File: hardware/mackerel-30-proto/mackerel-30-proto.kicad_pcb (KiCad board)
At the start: 2 copper layers, 24 parts, among them U1 MC68030RC, U2 EPM7128, U3 SST39SF040, U4 AS6C4008-55PCN

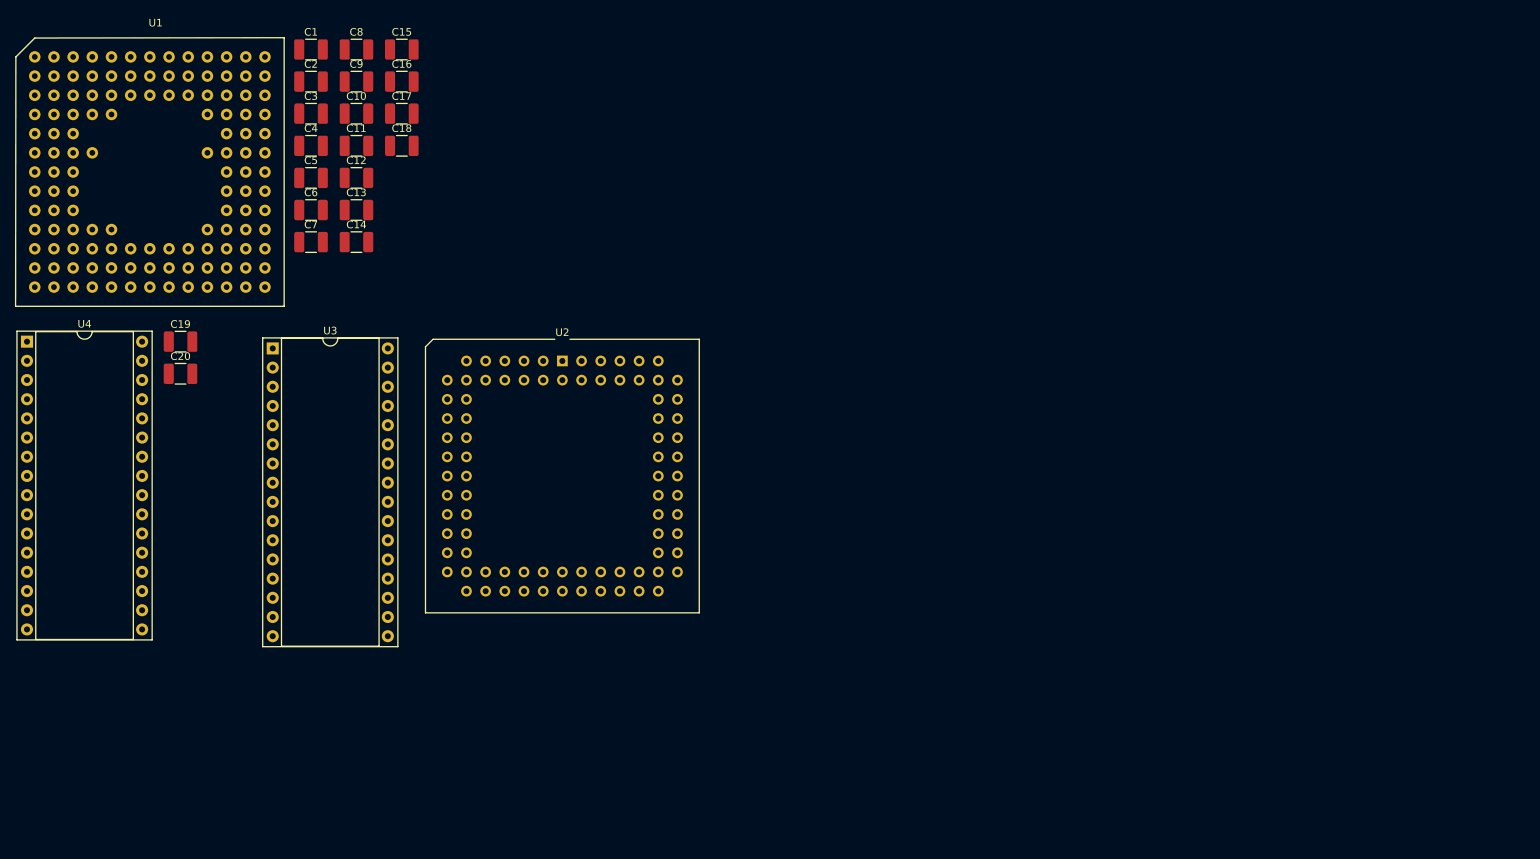
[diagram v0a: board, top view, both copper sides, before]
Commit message: Add power and DUART
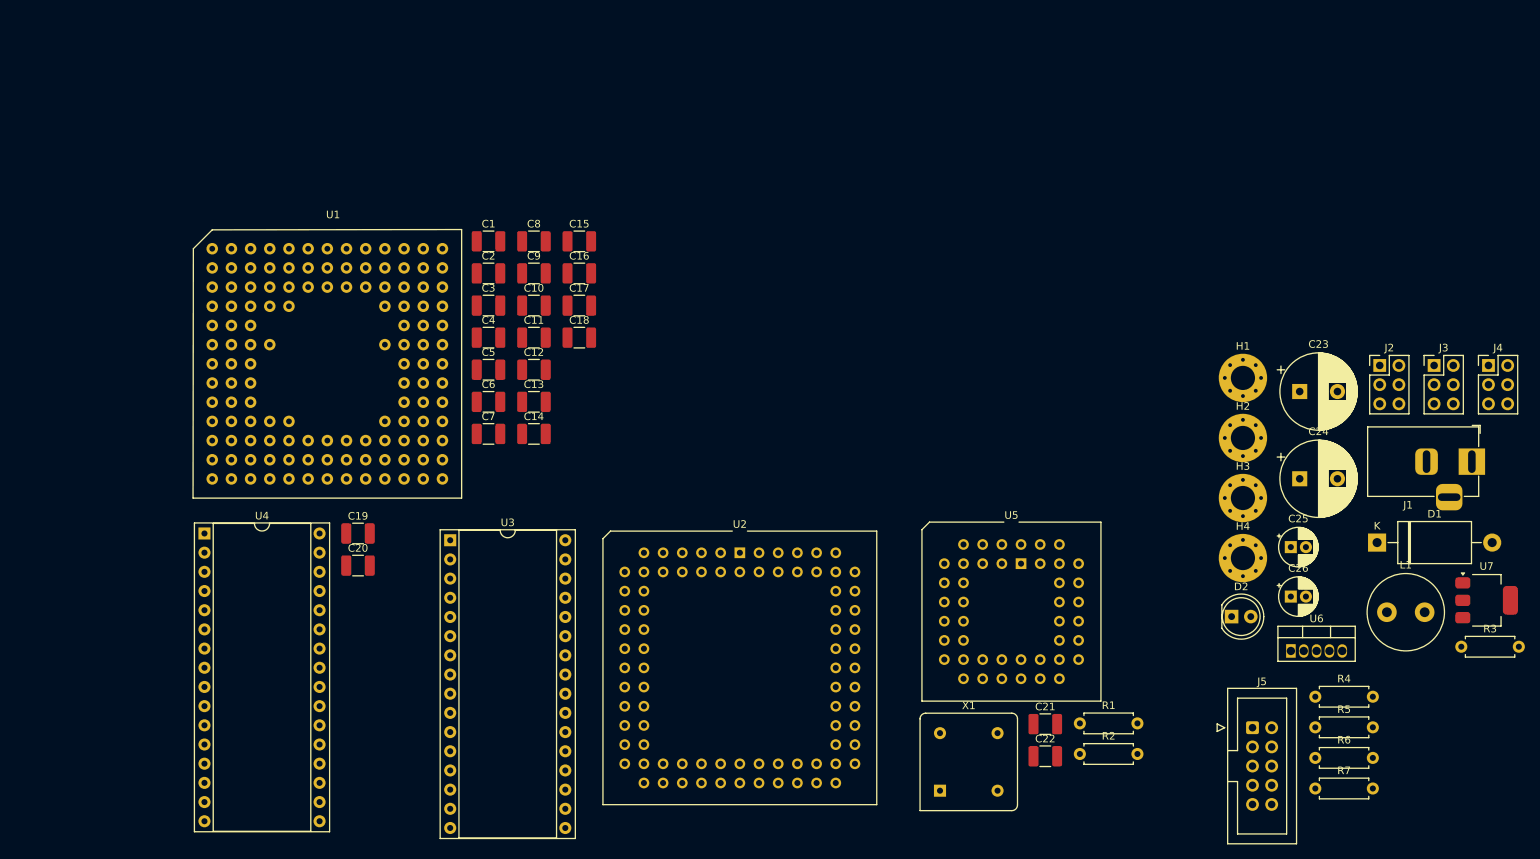
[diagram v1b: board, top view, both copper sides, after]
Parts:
- added C21: 0.1uF, Capacitor_SMD:C_1210_3225Metric_Pad1.33x2.70mm_HandSolder, F.Cu at (136.4, 90.9)
- added C22: 0.1uF, Capacitor_SMD:C_1210_3225Metric_Pad1.33x2.70mm_HandSolder, F.Cu at (136.4, 95.2)
- added C23: 1000uF, Capacitor_THT:CP_Radial_D10.0mm_P5.00mm, F.Cu at (170.1, 46.9)
- added C24: 1000uF, Capacitor_THT:CP_Radial_D10.0mm_P5.00mm, F.Cu at (170.1, 58.5)
- added C25: 10uF, Capacitor_THT:CP_Radial_D5.0mm_P2.00mm, F.Cu at (168.9, 67.5)
- added C26: 10uF, Capacitor_THT:CP_Radial_D5.0mm_P2.00mm, F.Cu at (168.9, 74.1)
- added D1: 1N5822, Diode_THT:D_DO-27_P15.24mm_Horizontal, F.Cu at (180.3, 66.9)
- added D2: LED, LED_THT:LED_D5.0mm, F.Cu at (161.1, 76.7)
- added H1: MountingHole_Pad, MountingHole:MountingHole_3.2mm_M3_Pad_Via, F.Cu at (162.6, 45.1)
- added H2: MountingHole_Pad, MountingHole:MountingHole_3.2mm_M3_Pad_Via, F.Cu at (162.6, 53.1)
- added H3: MountingHole_Pad, MountingHole:MountingHole_3.2mm_M3_Pad_Via, F.Cu at (162.6, 61.0)
- added H4: MountingHole_Pad, MountingHole:MountingHole_3.2mm_M3_Pad_Via, F.Cu at (162.6, 69.0)
- added J1: Barrel_Jack_MountingPin, Connector_BarrelJack:BarrelJack_Horizontal, F.Cu at (192.9, 56.2)
- added J2: Conn_02x03_Odd_Even, Connector_PinHeader_2.54mm:PinHeader_2x03_P2.54mm_Vertical, F.Cu at (180.7, 43.5)
- added J3: Conn_02x03_Odd_Even, Connector_PinHeader_2.54mm:PinHeader_2x03_P2.54mm_Vertical, F.Cu at (187.9, 43.5)
- added J4: Conn_02x03_Odd_Even, Connector_PinHeader_2.54mm:PinHeader_2x03_P2.54mm_Vertical, F.Cu at (195.1, 43.5)
- added J5: Conn_02x05_Odd_Even, Connector_IDC:IDC-Header_2x05_P2.54mm_Vertical, F.Cu at (163.8, 91.4)
- added L1: 100uH, Inductor_THT:L_Radial_D10.0mm_P5.00mm_Fastron_07M, F.Cu at (181.6, 76.1)
- added R1: R, Resistor_THT:R_Axial_DIN0207_L6.3mm_D2.5mm_P7.62mm_Horizontal, F.Cu at (141.0, 90.8)
- added R2: R, Resistor_THT:R_Axial_DIN0207_L6.3mm_D2.5mm_P7.62mm_Horizontal, F.Cu at (141.0, 94.9)
- added R3: 1k, Resistor_THT:R_Axial_DIN0207_L6.3mm_D2.5mm_P7.62mm_Horizontal, F.Cu at (191.5, 80.7)
- added R4: R, Resistor_THT:R_Axial_DIN0207_L6.3mm_D2.5mm_P7.62mm_Horizontal, F.Cu at (172.1, 87.3)
- added R5: R, Resistor_THT:R_Axial_DIN0207_L6.3mm_D2.5mm_P7.62mm_Horizontal, F.Cu at (172.1, 91.4)
- added R6: R, Resistor_THT:R_Axial_DIN0207_L6.3mm_D2.5mm_P7.62mm_Horizontal, F.Cu at (172.1, 95.4)
- added R7: R, Resistor_THT:R_Axial_DIN0207_L6.3mm_D2.5mm_P7.62mm_Horizontal, F.Cu at (172.1, 99.5)
- added U5: XR68C681, Package_LCC:PLCC-44_THT-Socket, F.Cu at (133.2, 69.7)
- added U6: LM2576T-5, Package_TO_SOT_THT:TO-220-5_Vertical, F.Cu at (168.9, 81.3)
- added U7: AMS1117-3.3, Package_TO_SOT_SMD:SOT-223-3_TabPin2, F.Cu at (194.8, 74.6)
- added X1: 3.6864MHz, Oscillator:Oscillator_DIP-8, F.Cu at (122.5, 99.8)
- moved U2 34.6 mm to (96.0, 68.3)
- moved C10 34.6 mm to (68.7, 35.5)
- moved C11 34.6 mm to (68.7, 39.8)
- moved C12 34.6 mm to (68.7, 44.0)
- moved C13 34.6 mm to (68.7, 48.3)
- moved C14 34.6 mm to (68.7, 52.5)
- moved C17 34.6 mm to (74.7, 35.5)
- moved C18 34.6 mm to (74.7, 39.8)
- moved C3 34.6 mm to (62.7, 35.5)
- moved C4 34.6 mm to (62.7, 39.8)
- moved C5 34.6 mm to (62.7, 44.0)
- moved C6 34.6 mm to (62.7, 48.3)
- moved C7 34.6 mm to (62.7, 52.5)
- moved U3 34.6 mm to (57.6, 66.6)
- moved C1 34.6 mm to (62.7, 27.0)
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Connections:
- U2 pad 14: unconnected-(U2-TDI-Pad14) -> TDI
- U2 pad 23: unconnected-(U2-TMS-Pad23) -> TMS
- U2 pad 62: unconnected-(U2-TCK-Pad62) -> TCK
- U2 pad 71: unconnected-(U2-TDO-Pad71) -> TDO

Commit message: Add 68882 FPU symbol
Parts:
- removed R5: R, Resistor_THT:R_Axial_DIN0207_L6.3mm_D2.5mm_P7.62mm_Horizontal
- added J6: Conn_02x05_Odd_Even, Connector_IDC:IDC-Header_2x05_P2.54mm_Vertical, F.Cu at (-90.8, 30.1)
- added R10: R, Resistor_THT:R_Axial_DIN0207_L6.3mm_D2.5mm_P7.62mm_Horizontal, F.Cu at (-82.5, 30.1)
- added R11: R, Resistor_THT:R_Axial_DIN0207_L6.3mm_D2.5mm_P7.62mm_Horizontal, F.Cu at (-82.5, 34.1)
- added R12: R, Resistor_THT:R_Axial_DIN0207_L6.3mm_D2.5mm_P7.62mm_Horizontal, F.Cu at (-82.5, 38.2)
- added R8: 1k, Resistor_THT:R_Axial_DIN0207_L6.3mm_D2.5mm_P7.62mm_Horizontal, F.Cu at (-38.4, 147.9)
- added R9: R, Resistor_THT:R_Axial_DIN0207_L6.3mm_D2.5mm_P7.62mm_Horizontal, F.Cu at (-82.5, 26.0)
- added U10: MC68882, Package_LCC:PLCC-68_THT-Socket, F.Cu at (-121.9, 59.7)
- added U8: EPM7128, Package_LCC:PLCC-84_THT-Socket, F.Cu at (176.4, 30.0)
- added U9: SIMM72, mackerel:SIMM-72, F.Cu at (208.6, 32.3)
- C24: value 1000uF -> 10uF; footprint Capacitor_THT:CP_Radial_D10.0mm_P5.00mm -> Capacitor_THT:CP_Radial_D5.0mm_P2.00mm
- C25: value 10uF -> 1000uF; footprint Capacitor_THT:CP_Radial_D5.0mm_P2.00mm -> Capacitor_THT:CP_Radial_D10.0mm_P5.00mm
- D1: value 1N5822 -> LED; footprint Diode_THT:D_DO-27_P15.24mm_Horizontal -> LED_THT:LED_D5.0mm
- D2: value LED -> 1N5822; footprint LED_THT:LED_D5.0mm -> Diode_THT:D_DO-27_P15.24mm_Horizontal
- J1: value Barrel_Jack_MountingPin -> Conn_02x05_Odd_Even; footprint Connector_BarrelJack:BarrelJack_Horizontal -> Connector_IDC:IDC-Header_2x05_P2.54mm_Vertical
- J2: value Conn_02x03_Odd_Even -> Barrel_Jack_MountingPin; footprint Connector_PinHeader_2.54mm:PinHeader_2x03_P2.54mm_Vertical -> Connector_BarrelJack:BarrelJack_Horizontal
- J5: value Conn_02x05_Odd_Even -> Conn_02x03_Odd_Even; footprint Connector_IDC:IDC-Header_2x05_P2.54mm_Vertical -> Connector_PinHeader_2.54mm:PinHeader_2x03_P2.54mm_Vertical
- R3: value 1k -> R
- U4: footprint Package_DIP:DIP-32_W15.24mm_Socket -> Package_DIP:DIP-32_W15.24mm
- moved J1 284.0 mm to (-90.8, 70.2)
- moved R3 274.1 mm to (-82.5, 74.2)
- moved D1 260.8 mm to (-68.8, 144.0)
- moved R4 254.8 mm to (-82.5, 78.2)
- moved J4 246.5 mm to (-42.0, 110.7)
- moved J3 246.5 mm to (-49.2, 110.7)
- moved C24 243.3 mm to (-61.0, 134.8)
- moved C23 239.5 mm to (-59.8, 114.2)
- moved C26 239.5 mm to (-61.0, 141.3)
- moved H1 239.5 mm to (-67.3, 112.4)
- moved H2 239.5 mm to (-67.3, 120.3)
- moved H3 239.5 mm to (-67.3, 128.3)
- moved H4 239.5 mm to (-67.3, 136.2)
- moved L1 239.5 mm to (-48.3, 143.4)
- moved U6 239.5 mm to (-61.0, 148.5)
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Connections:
- D1 pad 1: Net-(D1-K) -> GND
- D1 pad 2: GND -> Net-(D1-A)
- D2 pad 1: GND -> Net-(D2-K)
- D2 pad 2: Net-(D2-A) -> GND
- J1 pad 1: +12V -> TCK
- J1 pad 3: (no net) -> TDO
- J2 pad 3: +12V -> (no net)
- J3 pad 1: +5V -> +12V
- J3 pad 3: +5V -> +12V
- J3 pad 5: +5V -> +12V
- J4 pad 1: +3.3V -> +5V
- J4 pad 3: +3.3V -> +5V
- J4 pad 5: +3.3V -> +5V
- J5 pad 1: TCK -> +3.3V
- J5 pad 3: TDO -> +3.3V
- J5 pad 4: +5V -> GND
- J5 pad 5: TMS -> +3.3V
- J5 pad 6: unconnected-(J5-Pin_6-Pad6) -> GND
- L1 pad 1: Net-(D1-K) -> Net-(D2-K)
- R1 pad 1: Net-(U5-/IACK) -> +5V
- R1 pad 2: +5V -> TDO
- R2 pad 1: Net-(U5-INTR) -> +5V
- R2 pad 2: +5V -> TMS
- R3 pad 2: Net-(D2-A) -> TDI
- R4 pad 1: +5V -> TCK
- R4 pad 2: TDO -> GND
- R6 pad 1: +5V -> Net-(U5-/IACK)
- R6 pad 2: TDI -> +5V
- R7 pad 1: TCK -> Net-(U5-INTR)
- R7 pad 2: GND -> +5V
- U3 pad 22: unconnected-(U3-CE-Pad22) -> /CS_ROM
- U3 pad 24: unconnected-(U3-OE-Pad24) -> GND
- U3 pad 31: unconnected-(U3-PGM-Pad31) -> Net-(U3-PGM)
- U4 pad 22: unconnected-(U4-CE#-Pad22) -> /CS_SRAM
- U4 pad 24: unconnected-(U4-OE#-Pad24) -> GND
- U6 pad 2: Net-(D1-K) -> Net-(D2-K)
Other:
- board outline added: 200 x 120 mm

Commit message: Wired most of the control signals for the CPU and DRAM
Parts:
- removed J5: Conn_02x03_Odd_Even, Connector_PinHeader_2.54mm:PinHeader_2x03_P2.54mm_Vertical
- removed J6: Conn_02x05_Odd_Even, Connector_IDC:IDC-Header_2x05_P2.54mm_Vertical
- added J10: DE9_Plug_MountingHoles, Connector_Dsub:DSUB-9_Male_Horizontal_P2.77x2.84mm_EdgePinOffset7.70mm_Housed_MountingHolesOffset9.12mm, F.Cu at (30.8, 86.0)
- added J8: Conn_02x05_Odd_Even, Connector_IDC:IDC-Header_2x05_P2.54mm_Vertical, F.Cu at (260.9, 58.8)
- added J9: DE9_Plug_MountingHoles, Connector_Dsub:DSUB-9_Male_Horizontal_P2.77x2.84mm_EdgePinOffset7.70mm_Housed_MountingHolesOffset9.12mm, F.Cu at (30.8, 46.0)
- added R13: R, Resistor_THT:R_Axial_DIN0207_L6.3mm_D2.5mm_P7.62mm_Horizontal, F.Cu at (255.6, 119.6)
- added R14: 4k7, Resistor_THT:R_Axial_DIN0207_L6.3mm_D2.5mm_P7.62mm_Horizontal, F.Cu at (-97.8, 157.7)
- added R15: R, Resistor_THT:R_Axial_DIN0207_L6.3mm_D2.5mm_P7.62mm_Horizontal, F.Cu at (-91.7, 65.8)
- added R16: R, Resistor_THT:R_Axial_DIN0207_L6.3mm_D2.5mm_P7.62mm_Horizontal, F.Cu at (-91.7, 69.9)
- added R17: 1k, Resistor_THT:R_Axial_DIN0207_L6.3mm_D2.5mm_P7.62mm_Horizontal, F.Cu at (-77.5, 97.3)
- added R18: R, Resistor_THT:R_Axial_DIN0207_L6.3mm_D2.5mm_P7.62mm_Horizontal, F.Cu at (269.2, 54.6)
- added R19: R, Resistor_THT:R_Axial_DIN0207_L6.3mm_D2.5mm_P7.62mm_Horizontal, F.Cu at (269.2, 58.7)
- added R20: R, Resistor_THT:R_Axial_DIN0207_L6.3mm_D2.5mm_P7.62mm_Horizontal, F.Cu at (269.2, 62.8)
- added R21: R, Resistor_THT:R_Axial_DIN0207_L6.3mm_D2.5mm_P7.62mm_Horizontal, F.Cu at (269.2, 66.8)
- added R5: 4k7, Resistor_THT:R_Axial_DIN0207_L6.3mm_D2.5mm_P7.62mm_Horizontal, F.Cu at (-190.3, 82.0)
- added U11: MAX232, Package_DIP:DIP-16_W7.62mm_Socket, F.Cu at (112.1, -77.1)
- added U12: MAX232, Package_DIP:DIP-16_W7.62mm_Socket, F.Cu at (123.9, -77.1)
- added X2: 3.6864MHz, Oscillator:Oscillator_DIP-8, F.Cu at (139.7, -68.2)
- J1: value Conn_02x05_Odd_Even -> Conn_01x02; footprint Connector_IDC:IDC-Header_2x05_P2.54mm_Vertical -> Connector_PinHeader_2.54mm:PinHeader_1x02_P2.54mm_Vertical
- J2: value Barrel_Jack_MountingPin -> Conn_01x02; footprint Connector_BarrelJack:BarrelJack_Horizontal -> Connector_PinHeader_2.54mm:PinHeader_1x02_P2.54mm_Vertical
- J3: value Conn_02x03_Odd_Even -> Conn_02x05_Odd_Even; footprint Connector_PinHeader_2.54mm:PinHeader_2x03_P2.54mm_Vertical -> Connector_IDC:IDC-Header_2x05_P2.54mm_Vertical
- J4: value Conn_02x03_Odd_Even -> Barrel_Jack_MountingPin; footprint Connector_PinHeader_2.54mm:PinHeader_2x03_P2.54mm_Vertical -> Connector_BarrelJack:BarrelJack_Horizontal
- R1, R2, R3, R4, R6, R7, R9: value R -> 4k7
- R8: value 1k -> 4k7
- X1: value 3.6864MHz -> CXO_DIP14; footprint Oscillator:Oscillator_DIP-8 -> Oscillator:Oscillator_DIP-14
- moved R10 346.9 mm to (255.6, 107.5)
- moved R11 346.9 mm to (255.6, 111.5)
- moved R12 346.9 mm to (255.6, 115.5)
- moved J3 320.4 mm to (271.2, 108.8)
- moved H2 269.3 mm to (185.1, 26.4)
- moved H4 256.9 mm to (185.1, 183.8)
- moved U10 237.9 mm to (109.1, 116.7)
- moved U1 226.4 mm to (90.6, 58.7)
- moved U5 212.0 mm to (124.4, -46.5)
- moved U6 191.7 mm to (18.3, -26.0)
- moved R6 191.5 mm to (-190.3, 86.1)
- moved R7 191.5 mm to (-190.3, 90.2)
- moved L1 191.1 mm to (46.0, -22.8)
- moved C23 171.8 mm to (36.1, -28.4)
- moved C25 171.8 mm to (36.1, -16.8)
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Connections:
- J1 pad 1: TCK -> Net-(J1-Pin_1)
- J2 pad 1: +12V -> Net-(J2-Pin_1)
- J3 pad 1: +12V -> TCK
- J3 pad 3: +12V -> TDO
- J3 pad 4: GND -> +5V
- J3 pad 5: +12V -> TMS
- J3 pad 6: GND -> unconnected-(J3-Pin_6-Pad6)
- J4 pad 1: +5V -> +12V
- J4 pad 3: +5V -> (no net)
- R1 pad 2: TDO -> Net-(J2-Pin_1)
- R10 pad 2: TMS_DRAM -> TDO
- R11 pad 2: TDI_DRAM -> TMS
- R12 pad 1: TCK_DRAM -> +5V
- R12 pad 2: GND -> TDI
- R2 pad 2: TMS -> Net-(U1-/CBACK)
- R3 pad 2: TDI -> Net-(J1-Pin_1)
- R4 pad 1: TCK -> +5V
- R4 pad 2: GND -> Net-(U1-/HALT)
- R6 pad 1: Net-(U5-/IACK) -> +5V
- R6 pad 2: +5V -> /IPL1
- R7 pad 1: Net-(U5-INTR) -> +5V
- R7 pad 2: +5V -> /IPL2
- R8 pad 2: Net-(D1-A) -> Net-(U1-/BR)
- R9 pad 2: TDO_DRAM -> Net-(U1-/BGACK)
- U1 pad A1: unconnected-(U1-/BR-PadA1) -> Net-(U1-/BR)
- U1 pad A3: A30 -> unconnected-(U1-A30-PadA3)
- U1 pad A4: A28 -> unconnected-(U1-A28-PadA4)
- U1 pad B3: A31 -> unconnected-(U1-A31-PadB3)
- U1 pad B4: A29 -> unconnected-(U1-A29-PadB4)
- U1 pad C3: unconnected-(U1-/BGACK-PadC3) -> Net-(U1-/BGACK)
- U1 pad E1: unconnected-(U1-CLK-PadE1) -> CLK_CPU
- U1 pad F12: unconnected-(U1-/RESET-PadF12) -> /RESET
- U1 pad F13: unconnected-(U1-/MMUDIS-PadF13) -> Net-(J1-Pin_1)
- U1 pad G1: unconnected-(U1-/STERM-PadG1) -> /STERM
- U1 pad H1: unconnected-(U1-/BERR-PadH1) -> /BERR
- U1 pad H12: unconnected-(U1-/CDIS-PadH12) -> Net-(J2-Pin_1)
- U1 pad H2: unconnected-(U1-/HALT-PadH2) -> Net-(U1-/HALT)
- U1 pad J1: unconnected-(U1-/CBACK-PadJ1) -> Net-(U1-/CBACK)
- U1 pad L1: unconnected-(U1-/CIIN-PadL1) -> /CIIN
- U10 pad 13: unconnected-(U10-/RESET-Pad13) -> /RESET
- U10 pad 29: unconnected-(U10-/CS-Pad29) -> /CS_FPU
- U10 pad 31: unconnected-(U10-/DSACK0-Pad31) -> /DSACK0_FPU
- U10 pad 32: unconnected-(U10-/DSACK1-Pad32) -> /DSACK1_FPU
- U2 pad 10: unconnected-(U2-IO-Pad10) -> /CS_DRAM
- U2 pad 11: unconnected-(U2-IO-Pad11) -> /DTACK_DRAM
- U2 pad 12: unconnected-(U2-IO-Pad12) -> /CS_DUART
- U2 pad 15: unconnected-(U2-IO-Pad15) -> /DTACK_DUART
- U2 pad 16: unconnected-(U2-IO-Pad16) -> /IRQ_DUART
- U2 pad 17: unconnected-(U2-IO-Pad17) -> /IACK_DUART
- U2 pad 18: unconnected-(U2-IO-Pad18) -> IDE_INT
- U2 pad 20: unconnected-(U2-IO-Pad20) -> /IDE_CS0
- U2 pad 21: unconnected-(U2-IO-Pad21) -> IDE_RDY
- U2 pad 22: unconnected-(U2-IO-Pad22) -> /IDE_RD
- U2 pad 24: unconnected-(U2-IO-Pad24) -> /IDE_WR
- U2 pad 25: unconnected-(U2-IO-Pad25) -> /IDE_BUF
- U2 pad 27: unconnected-(U2-IO-Pad27) -> /CS_FPU
- U2 pad 28: unconnected-(U2-IO-Pad28) -> /DSACK0_FPU
- U2 pad 29: unconnected-(U2-IO-Pad29) -> /DSACK1_FPU
- U2 pad 33: unconnected-(U2-IO-Pad33) -> D24
- U2 pad 34: unconnected-(U2-IO-Pad34) -> D25
- U2 pad 35: unconnected-(U2-IO-Pad35) -> D26
- U2 pad 36: unconnected-(U2-IO-Pad36) -> D27
- U2 pad 37: unconnected-(U2-IO-Pad37) -> D28
- U2 pad 39: unconnected-(U2-IO-Pad39) -> D29
- U2 pad 4: unconnected-(U2-IO-Pad4) -> /CIIN
- U2 pad 40: unconnected-(U2-IO-Pad40) -> D30
- U2 pad 41: unconnected-(U2-IO-Pad41) -> D31
- U2 pad 44: unconnected-(U2-IO-Pad44) -> A0
- U2 pad 45: unconnected-(U2-IO-Pad45) -> A1
- U2 pad 46: unconnected-(U2-IO-Pad46) -> A2
- U2 pad 48: unconnected-(U2-IO-Pad48) -> A3
- U2 pad 49: unconnected-(U2-IO-Pad49) -> A16
- U2 pad 5: unconnected-(U2-IO-Pad5) -> /STERM
- U2 pad 50: unconnected-(U2-IO-Pad50) -> A17
- U2 pad 51: unconnected-(U2-IO-Pad51) -> A18
- U2 pad 52: unconnected-(U2-IO-Pad52) -> A19
- U2 pad 54: unconnected-(U2-IO-Pad54) -> A20
- U2 pad 55: unconnected-(U2-IO-Pad55) -> A21
- U2 pad 56: unconnected-(U2-IO-Pad56) -> A22
- U2 pad 57: unconnected-(U2-IO-Pad57) -> A23
- U2 pad 58: unconnected-(U2-IO-Pad58) -> A24
- U2 pad 6: unconnected-(U2-IO-Pad6) -> /BERR
- U2 pad 60: unconnected-(U2-IO-Pad60) -> A25
- U2 pad 61: unconnected-(U2-IO-Pad61) -> A26
- U2 pad 63: unconnected-(U2-IO-Pad63) -> A27
- U2 pad 64: unconnected-(U2-IO-Pad64) -> /AS
- U2 pad 65: unconnected-(U2-IO-Pad65) -> /DS
- U2 pad 67: unconnected-(U2-IO-Pad67) -> R/W
- U2 pad 68: unconnected-(U2-IO-Pad68) -> /DSACK0
- U2 pad 69: unconnected-(U2-IO-Pad69) -> /DSACK1
- U2 pad 70: unconnected-(U2-IO-Pad70) -> SIZ0
- U2 pad 73: unconnected-(U2-IO-Pad73) -> SIZ1
- U2 pad 74: unconnected-(U2-IO-Pad74) -> /IPL0
- U2 pad 75: unconnected-(U2-IO-Pad75) -> /IPL1
- U2 pad 76: unconnected-(U2-IO-Pad76) -> /IPL2
- U2 pad 77: unconnected-(U2-IO-Pad77) -> FC0
- U2 pad 79: unconnected-(U2-IO-Pad79) -> FC1
- U2 pad 8: unconnected-(U2-IO-Pad8) -> /CS_ROM
- U2 pad 80: unconnected-(U2-IO-Pad80) -> FC2
- U2 pad 81: unconnected-(U2-IO-Pad81) -> /AVEC
- U2 pad 83: unconnected-(U2-GCLK1-Pad83) -> CLK_CPU
- U2 pad 9: unconnected-(U2-IO-Pad9) -> /CS_SRAM
- U5 pad 10: unconnected-(U5-/DTACK-Pad10) -> /DTACK_DUART
- U5 pad 24: Net-(U5-INTR) -> /IRQ_DUART
- U5 pad 38: unconnected-(U5-/RESET-Pad38) -> /RESET
- U5 pad 39: unconnected-(U5-CS-Pad39) -> /CS_DUART
- U5 pad 41: Net-(U5-/IACK) -> /IACK_DUART
- U8 pad 68: unconnected-(U8-IO-Pad68) -> A27
- X1 pad 8: +5V -> CLK_CPU
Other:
- board size 200 x 120 mm -> 170 x 170 mm

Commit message: A bit of cleanup
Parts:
- removed J10, J9: DE9_Plug_MountingHoles, Connector_Dsub:DSUB-9_Male_Horizontal_P2.77x2.84mm_EdgePinOffset7.70mm_Housed_MountingHolesOffset9.12mm
- removed U11, U12: MAX232, Package_DIP:DIP-16_W7.62mm_Socket
- added R4: 4k7, Resistor_THT:R_Axial_DIN0207_L6.3mm_D2.5mm_P7.62mm_Horizontal, F.Cu at (-102.8, 26.5)
- added X3: CXO_DIP14, Oscillator:Oscillator_DIP-14, F.Cu at (-100.9, 19.2)
- moved H4 376.5 mm to (-126.9, -26.9)
- moved H2 319.6 mm to (-126.9, -42.8)
- moved H3 269.2 mm to (-126.9, -34.8)
- moved H1 195.7 mm to (-126.9, -50.7)
- moved J4 161.5 mm to (-108.4, -49.3)
- moved U8 121.0 mm to (44.5, 39.1)
- moved U2 101.4 mm to (88.4, 39.5)
- moved U10 38.9 mm to (130.1, 84.0)
- moved U9 33.8 mm to (39.2, 23.3)
- moved U1 30.8 mm to (114.6, 39.3)
- moved U3 24.2 mm to (69.2, 112.2), turned to 90 degrees
- moved U4 17.1 mm to (69.1, 93.3), turned to 90 degrees
- renumbered J8 to J5, R9 to R10, R10 to R11, R11 to R12, R12 to R13, R13 to R14, R14 to R15, R15 to R16, R16 to R17, R17 to R18, R18 to R19, R19 to R20, R20 to R21, R21 to R22, R4 to R5, R5 to R6, R6 to R7, R7 to R8, R8 to R9
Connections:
- U1 pad H1: /BERR -> Net-(U1-/BERR)
- U2 pad 33: D24 -> unconnected-(U2-IO-Pad33)
- U2 pad 34: D25 -> unconnected-(U2-IO-Pad34)
- U2 pad 35: D26 -> unconnected-(U2-IO-Pad35)
- U2 pad 36: D27 -> unconnected-(U2-IO-Pad36)
- U2 pad 37: D28 -> unconnected-(U2-IO-Pad37)
- U2 pad 39: D29 -> unconnected-(U2-IO-Pad39)
- U2 pad 40: D30 -> unconnected-(U2-IO-Pad40)
- U2 pad 41: D31 -> unconnected-(U2-IO-Pad41)
- U2 pad 6: /BERR -> unconnected-(U2-IO-Pad6)
- U8 pad 10: unconnected-(U8-IO-Pad10) -> R/W
- U8 pad 11: unconnected-(U8-IO-Pad11) -> SIZ0
- U8 pad 12: unconnected-(U8-IO-Pad12) -> SIZ1
- U8 pad 2: unconnected-(U8-OE2/GCLK2-Pad2) -> CLK_CPU
- U8 pad 4: unconnected-(U8-IO-Pad4) -> /RESET
- U8 pad 5: unconnected-(U8-IO-Pad5) -> /CS_DRAM
- U8 pad 6: unconnected-(U8-IO-Pad6) -> /DTACK_DRAM
- U8 pad 8: unconnected-(U8-IO-Pad8) -> /AS
- U8 pad 83: unconnected-(U8-GCLK1-Pad83) -> CLK_DRAM
- U8 pad 9: unconnected-(U8-IO-Pad9) -> /DS
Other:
- board size 170 x 170 mm -> 160 x 100 mm
